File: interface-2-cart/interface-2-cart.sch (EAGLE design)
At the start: 37 parts, among them U1 RP2040, U2 SN74LVC245ADBR, U3 W25Q128JVSIQ, U4 SN74LVC245ADBR, U5 SN74LVC245ADBR, X1 TSX-32250

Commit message: New images
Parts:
- added PROG: (no value), adafruit:PINHD-1X6
- added Q1, Q2: (no value), semicon-smd-ipc:NPN-TRANSISTOR_SOT23
- added R1, R10, R11, R12, R13, R14, R15, R16, R17, R18, R19, R2, R20, R5: 1K, rcl:R-EU_R0402
- added R4, R6: 10K, rcl:R-EU_R0402
- added RST_BUT: PTS645SM43SMTR92LFS, PTS645SM43SMTR92LFS:PTS645SM43SMTR92LFS
- added S_LED1, S_LED10, S_LED2, S_LED3, S_LED362, S_LED4, S_LED5, S_LED6, S_LED7, S_LED8, S_LED9: 20mA, led-0402:VLMW1500-GS08
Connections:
- removed net BUT: U1.GPIO22
- removed net RESET_5V: U5.A1
- removed net ROMCS: U1.GPIO27/ADC1, U2.DIR
- new net /CARTCS: R1.1, R6.2, S_LED8.C, U1.GPIO27/ADC1
- new net /RESET: PROG.4, Q2.C, R4.2, RST_BUT.3
- new net CARTCS: Q1.C, R5.2, U$1./ROMCS, U2.DIR
- new net L0: R10.1, S_LED7.A
- new net L1: R11.1, S_LED6.A
- new net L2: R12.1, S_LED5.A
- new net L3: R13.1, S_LED4.A
- new net L4: R14.1, S_LED3.A
- new net L5: R15.1, S_LED2.A
- new net L6: R16.1, S_LED1.A
- new net L7: R17.1, S_LED362.A
- new net N$1: Q1.B, R1.2
- new net N$2: Q2.B, R2.2
- new net N$4: R18.1, S_LED8.A
- new net N$5: R19.1, S_LED9.A
- new net N$6: R20.1, S_LED10.A
- new net SWCLK: PROG.2, U1.SWCLK
- new net SWD: PROG.3, U1.SWD
- new net USER_LED: R20.2, U1.GPIO22
- net 3V3: now also PROG.1, R6.1; no longer C2.2, U2.VCC
- net D0: now also R10.2
- net D1: now also R11.2
- net D2: now also R12.2
- net D3: now also R13.2
- net D4: now also R14.2
- net D5: now also R15.2
- net D6: now also R16.2
- net D7: now also R17.2
- net GND: now also PROG.6, Q1.E, Q2.E, RST_BUT.1, S_LED1.C, S_LED10.C, S_LED2.C, S_LED3.C, S_LED362.C, S_LED4.C, S_LED5.C, S_LED6.C, S_LED7.C, U5.B1
- net RESET: now also R2.1; no longer U5.B1
- net ROMRQ_5V: now also S_LED9.C
- net VCC: now also C2.2, PROG.5, R18.2, R19.2, R4.1, R5.1, U2.VCC; no longer U$1./ROMCS
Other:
- moved on the sheet: BOOT_BUT, C1, C5, R8, R9, RUN_BUT, X1

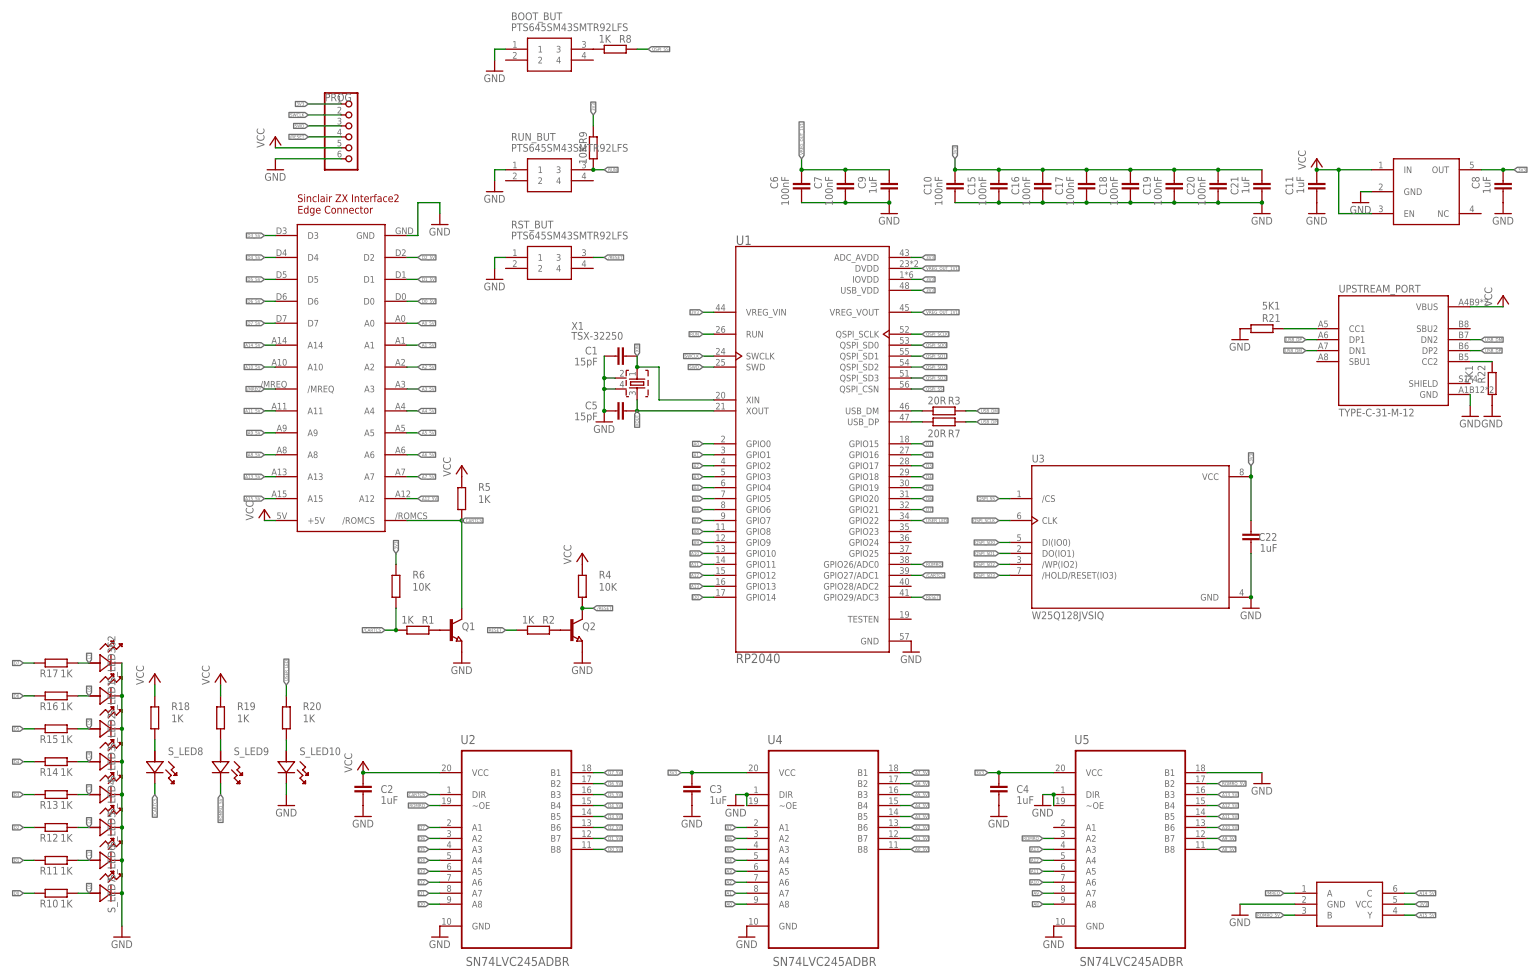
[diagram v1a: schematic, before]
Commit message: Created initial BOM and mount files, although need to replace one of the octal buffers with a level shifter
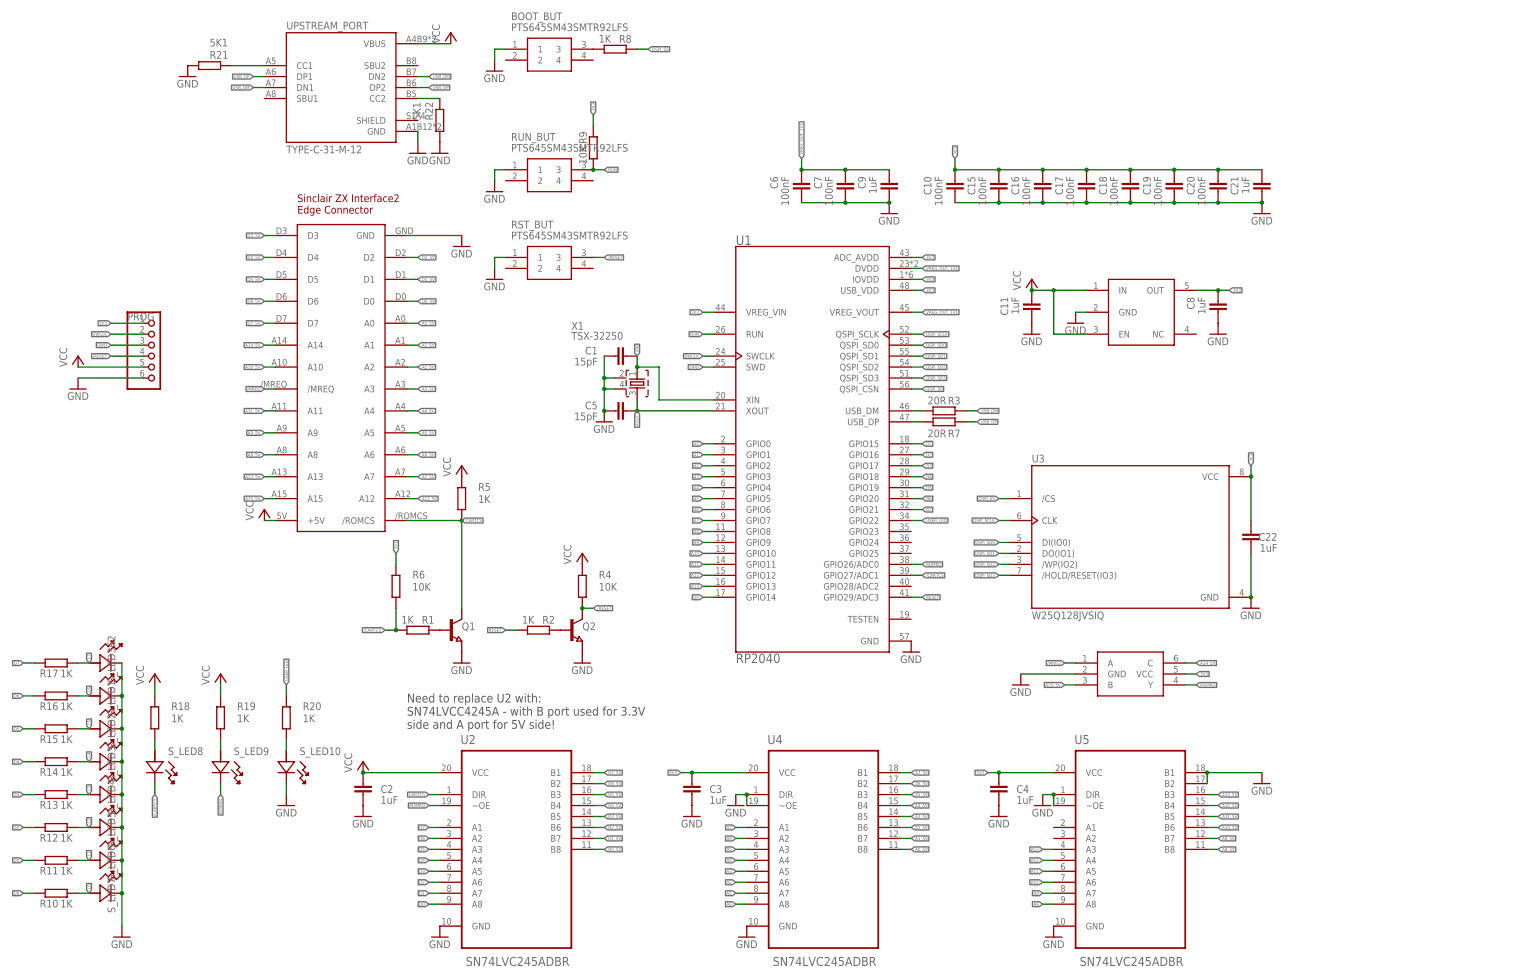
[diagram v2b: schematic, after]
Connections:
- removed net ROMRQ_5V: S_LED9.C, U$2.B, U5.B2
- net A15_5V: now also U$2.B; no longer U$2.Y
- net GND: now also U5.B2
- net ROMRQ: now also S_LED9.C, U$2.Y; no longer U5.A2
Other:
- note added: "Need to replace U2 with: SN74LVCC4245A - with B port used for 3.3V side and A port for 5V side!"
- moved on the sheet: C11, C8, PROG, R21, R22, UPSTREAM_PORT

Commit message: Fixed hardware issue! Fixed firmware issue with volatiles not updating - core1 was not starting up!
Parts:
- removed U2: SN74LVC245ADBR, SN74LVC245ADBR:SN74LVC245ADBR
- added C12: 1uF, rcl:C-EUC0402
- added D1, D2: BZX384C5V6-E3-08, BZX384C5V6-E3-08:BZX384C5V6-E3-08
- added U6: SN74LVCC4245APWR, SN74LVCC4245APWR:SN74LVCC4245APWR
- R5: value 1K -> 470R
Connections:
- new net /RESET_PROTECTED: D1.C, Q2.C, R4.2
- new net N$7: D2.C, U$1./ROMCS
- net /CARTCS: now also U6.DIR
- net /RESET: now also D1.A; no longer Q2.C, R4.2
- net 3V3: now also C12.2, U6.VCCB
- net CARTCS: now also D2.A; no longer U$1./ROMCS, U2.DIR
- net D0: now also U6.B1; no longer U2.A8
- net D0_5V: now also U6.A1; no longer U2.B8
- net D1: now also U6.B2; no longer U2.A7
- net D1_5V: now also U6.A2; no longer U2.B7
- net D2: now also U6.B3; no longer U2.A6
- net D2_5V: now also U6.A3; no longer U2.B6
- net D3: now also U6.B4; no longer U2.A5
- net D3_5V: now also U6.A4; no longer U2.B5
- net D4: now also U6.B5; no longer U2.A4
- net D4_5V: now also U6.A5; no longer U2.B4
- net D5: now also U6.B6; no longer U2.A3
- net D5_5V: now also U6.A6; no longer U2.B3
- net D6: now also U6.B7; no longer U2.A2
- net D6_5V: now also U6.A7; no longer U2.B2
- net D7: now also U6.B8; no longer U2.A1
- net D7_5V: now also U6.A8; no longer U2.B1
- net GND: now also C12.1, U6.GND, U6.GND-1, U6.GND-2; no longer U2.GND
- net ROMRQ: now also U6./OE; no longer U2.~OE
- net VCC: now also U6.VCCA; no longer U2.VCC
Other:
- note removed: "Need to replace U2 with: SN74LVCC4245A - with B port used for 3.3V side and A port for 5V side!"
- moved on the sheet: C2

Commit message: New cartridge PCB design, smaller, using RP2350 now. Need to modify more to reduce wings on side, so it's square I think - will give more space in casing
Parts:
- removed BOOT_BUT, RST_BUT, RUN_BUT: PTS645SM43SMTR92LFS, PTS645SM43SMTR92LFS:PTS645SM43SMTR92LFS
- removed C6, C7: 100nF, rcl:C-EUC0402
- removed C9: 1uF, rcl:C-EUC0402
- removed D1: BZX384C5V6-E3-08, BZX384C5V6-E3-08:BZX384C5V6-E3-08
- removed Q1, Q2: (no value), semicon-smd-ipc:NPN-TRANSISTOR_SOT23
- removed R1, R10, R11, R12, R13, R14, R15, R16, R17, R18, R19, R2, R8: 1K, rcl:R-EU_R0402
- removed R21, R22: 5K1, rcl:R-EU_R0402
- removed R3, R7: 20R, rcl:R-EU_R0402
- removed R4, R6: 10K, rcl:R-EU_R0402
- removed R5: 470R, rcl:R-EU_R0402
- removed S_LED1, S_LED2, S_LED3, S_LED362, S_LED4, S_LED5, S_LED6, S_LED7, S_LED8, S_LED9: 20mA, led-0402:VLMW1500-GS08
- removed U1: RP2040, RP2040:RP2040
- removed UPSTREAM_PORT: TYPE-C-31-M-12, TYPE-C-31-M-12:TYPE-C-31-M-12
- removed X1: TSX-32250, TSX-3225:TSX-32250
- added C13, C14: 15pF, res-small-footprint:CAP-0402
- added C23, C24: 2u2, res-small-footprint:CAP-0402
- added C25, C26, C28: 10uF, res-small-footprint:CAP-0402
- added C27: 100nF, res-small-footprint:CAP-0402
- added D3: BZX384C5V6-E3-08, BZX384C5V6-E3-08:BZX384C5V6-E3-08
- added L1: DFE252012F-3R3M=P2, microbuilder:INDUCTOR
- added R23: 1K, res-small-footprint:RES-0402
- added R24: 10K, res-small-footprint:RES-0402
- added R25: 10R, res-small-footprint:RES-0402
- added X2: TSX-32250, TSX-3225:TSX-32250
- added X3: DNP, adafruit_micro:RP2350_QFN60
- C1, C5: value 15pF -> 100nF; device rcl:C-EUC0402 -> res-small-footprint:CAP-0402
- C10, C11, C12, C15, C16, C17, C18, C19, C2, C20, C21, C22, C3, C4, C8: device rcl:C-EUC0402 -> res-small-footprint:CAP-0402
- R20: device rcl:R-EU_R0402 -> res-small-footprint:RES-0402
- R9: value 10K -> 10R; device rcl:R-EU_R0402 -> res-small-footprint:RES-0402
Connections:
- net N$7 renamed /ROMCS
- removed net /CARTCS: R1.1, R6.2, S_LED8.C, U1.GPIO27/ADC1, U6.DIR
- removed net /RESET_PROTECTED: D1.C, Q2.C, R4.2
- removed net CARTCS: D2.A, Q1.C, R5.2
- removed net L0: R10.1, S_LED7.A
- removed net L1: R11.1, S_LED6.A
- removed net L2: R12.1, S_LED5.A
- removed net L3: R13.1, S_LED4.A
- removed net L4: R14.1, S_LED3.A
- removed net L5: R15.1, S_LED2.A
- removed net L6: R16.1, S_LED1.A
- removed net L7: R17.1, S_LED362.A
- removed net N$1: Q1.B, R1.2
- removed net N$18: R21.2, UPSTREAM_PORT.CC1
- removed net N$19: R22.2, UPSTREAM_PORT.CC2
- removed net N$2: Q2.B, R2.2
- removed net N$3: R3.1, U1.USB_DM
- removed net N$4: R18.1, S_LED8.A
- removed net N$5: R19.1, S_LED9.A
- removed net N$8: R7.1, U1.USB_DP
- removed net RESET: R2.1, U1.GPIO29/ADC3
- removed net USB_DM: R3.2, UPSTREAM_PORT.DN1, UPSTREAM_PORT.DN2
- removed net USB_DP: R7.2, UPSTREAM_PORT.DP1, UPSTREAM_PORT.DP2
- removed net VREG_OUT_1V1: C6.1, C7.1, C9.1, U1.DVDD, U1.VREG_VOUT
- new net /RESET_3V3: U5.B2, X3.GPIO29/AD3
- new net /ROMCS_3V3: D2.A, U6.DIR, X3.GPIO27/AD1
- new net 1V2: C1.1, C27.1, C28.1, C5.1, L1.1, X3.DVDD, X3.VREG_FB
- new net N$10: R23.2, X3.XOUT
- new net N$11: L1.2, X3.VREG_LX
- new net N$12: C23.1, R9.1, X3.VREG_AVDD
- new net N$13: C24.1, R25.1, X3.ADC_AVDD
- new net ROMRQ_3V3: U5.A1, U6./OE, X3.GPIO26/AD0
- net /RESET: now also D3.A; no longer D1.A, RST_BUT.3
- net 3V3: now also C26.1, R24.2, R25.2, X3.IOVDD, X3.QSPI_IOVDD, X3.USB_OTP_VDD, X3.VREG_VIN; no longer R6.1, U1.ADC_AVDD, U1.IOVDD, U1.USB_VDD, U1.VREG_VIN
- net A0: now also X3.XPI_CS1/MISO0/TX0/SDA0/PWM0A/GPIO0; no longer U1.GPIO0
- net A1: now also X3.CS0/RX0/SCL0/PWM0B/GPIO1; no longer U1.GPIO1
- net A10: now also X3.SCK1/CTS1/SDA1/PWM5A/GPIO10; no longer U1.GPIO10
- net A11: now also X3.MOSI1/RTS1/SCL1/PWM5B/GPIO11; no longer U1.GPIO11
- net A12: now also X3.HSTX/MISO1/TX0/SDA0/PWM6A/GPIO12; no longer U1.GPIO12
- net A13: now also X3.HSTX/CS1/RX0/SCL0/PWM6B/GPIO13; no longer U1.GPIO13
- net A2: now also X3.SCK0/CTS0/SDA1/PWM1A/GPIO2; no longer U1.GPIO2
- net A3: now also X3.MOSI0/RTS0/SCL1/PWM1B/GPIO3; no longer U1.GPIO3
- net A4: now also X3.MISO0/TX1/SDA0/PWM2A/GPIO4; no longer U1.GPIO4
- net A5: now also X3.CS0/RX1/SCL0/PWM2B/GPIO5; no longer U1.GPIO5
- net A6: now also X3.SCK0/CTS1/SDA1/PWM3A/GPIO6; no longer U1.GPIO6
- net A7: now also X3.MOSI0/RTS1/SCL1/PWM3B/GPIO7; no longer U1.GPIO7
- net A8: now also X3.XIP_CS1/MISO1/TX1/SDA0/PWM4A/GPIO8; no longer U1.GPIO8
- net A9: now also X3.CS1/RX1/SCL0/PWM4B/GPIO9; no longer U1.GPIO9
- net D0: now also X3.HSTX/SCK1/CTS0/SDA1/PWM7A/GPIO14; no longer R10.2, U1.GPIO14
- net D1: now also X3.HSTX/MOSI1/RTS0/SCL1/PWM7B/GPIO15; no longer R11.2, U1.GPIO15
- net D2: now also X3.HSTX/MISO0/TX0/SDA0/PWM0A/GPIO16; no longer R12.2, U1.GPIO16
- net D3: now also X3.HSTX/CS0/RX0/SCL0/PWM0B/GPIO17; no longer R13.2, U1.GPIO17
- net D4: now also X3.HSTX/SCK0/CTS0/SDA1/PWM1A/GPIO18; no longer R14.2, U1.GPIO18
- net D5: now also X3.XPI_CS1/HSTX/MOSI0/RTS0/SCL1/PWM1B/GPIO19; no longer R15.2, U1.GPIO19
- net D6: now also X3.MISO0/TX1/SDA0/PWM2A/GPIO20; no longer R16.2, U1.GPIO20
- net D7: now also X3.CS0/RX1/SCL0/PWM2B/GPIO21; no longer R17.2, U1.GPIO21
- net GND: now also C13.2, C14.2, C23.2, C24.2, C25.2, C26.2, C27.2, C28.2, X2.2, X2.4, X3.GND, X3.VREG_PGND; no longer BOOT_BUT.1, C6.2, C7.2, C9.2, Q1.E, Q2.E, R21.1, R22.1, RST_BUT.1, RUN_BUT.1, S_LED1.C, S_LED2.C, S_LED3.C, S_LED362.C, S_LED4.C, S_LED5.C, S_LED6.C, S_LED7.C, U1.GND, U5.B1, U5.B2, UPSTREAM_PORT.GND, X1.2, X1.4
- net N$9: now also D3.C, U5.A2; no longer BOOT_BUT.3, R8.1
- net QSPI_SCLK: now also X3.QSPI_SCLK; no longer U1.QSPI_SCLK
- net QSPI_SD0: now also X3.QSPI_SD0; no longer U1.QSPI_SD0
- net QSPI_SD1: now also X3.QSPI_SD1; no longer U1.QSPI_SD1
- net QSPI_SD2: now also X3.QSPI_SD2; no longer U1.QSPI_SD2
- net QSPI_SD3: now also X3.QSPI_SD3; no longer U1.QSPI_SD3
- net QSPI_SS: now also X3.!QSPI_CS; no longer R8.2, U1.QSPI_CSN
- net ROMRQ: now also U5.B1; no longer S_LED9.C, U1.GPIO26/ADC0, U6./OE
- net RUN: now also R24.1, X3./RUN; no longer R9.1, RUN_BUT.3, U1.RUN
- net SWCLK: now also PROG.3, X3.SWCLK; no longer PROG.2, U1.SWCLK
- net SWD: now also PROG.2, X3.SWDIO; no longer PROG.3, U1.SWD
- net USER_LED: now also X3.SCK0/CTS1/SDA1/PWM3A/GPIO22; no longer U1.GPIO22
- net VCC: now also C25.1; no longer R18.2, R19.2, R4.1, R5.1, UPSTREAM_PORT.VBUS
- net XIN: now also C13.1, X2.1, X3.XIN; no longer C1.1, U1.XIN, X1.1
- net XOUT: now also C14.1, R23.1, X2.3; no longer C5.1, U1.XOUT, X1.3
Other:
- moved on the sheet: D2, S_LED10, U3, U5

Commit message: PCB design completed and submitted for production
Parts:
- removed PROG: (no value), adafruit:PINHD-1X6
- added JP2: (no value), pinhead:PINHD-1X5
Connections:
- net /RESET: now also JP2.4; no longer PROG.4
- net 3V3: now also JP2.1; no longer PROG.1
- net GND: now also JP2.5; no longer PROG.6
- net SWCLK: now also JP2.3; no longer PROG.3
- net SWD: now also JP2.2; no longer PROG.2
- net VCC: no longer PROG.5
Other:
- moved on the sheet: C1, C10, C11, C12, C13, C14, C15, C16, C17, C18, C19, C2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
